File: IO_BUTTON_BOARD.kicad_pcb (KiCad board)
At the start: 2 copper layers, 80 x 40 mm, 113 parts, among them P1 I2C, P10 IO_7, P2 I2C, P3 IO_0, P4 IO_1, P5 IO_2, P6 IO_3, P7 IO_4, P8 IO_5, P9 IO_6, Q1 NPN, Q10 PNP, Q11 PNP, Q12 PNP, Q13 PNP, Q2 PNP, Q3 NPN, Q4 PNP, Q5 NPN, Q6 PNP, Q7 PNP, Q8 PNP, Q9 PNP, SW1 I2C_ADDR, SW2 SW_0, SW3 SW_1, SW4 SW_2, SW5 SW_3, SW6 SW_4, SW7 SW_5, SW8 SW_6, SW9 SW_7, U1 PCF8574A, U2 74HC86, U3 74HC86

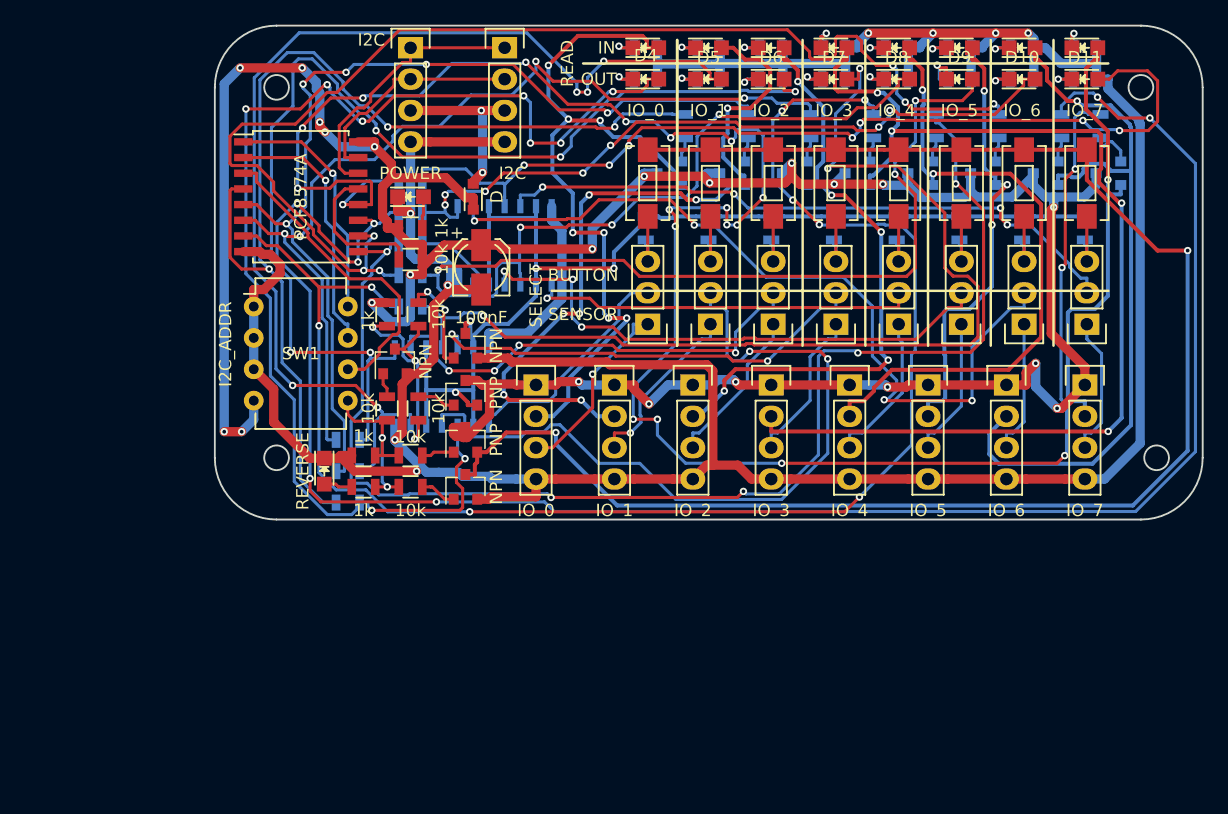
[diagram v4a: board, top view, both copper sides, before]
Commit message: Change positions of components Add mounting holes footprints Rerouted PCB
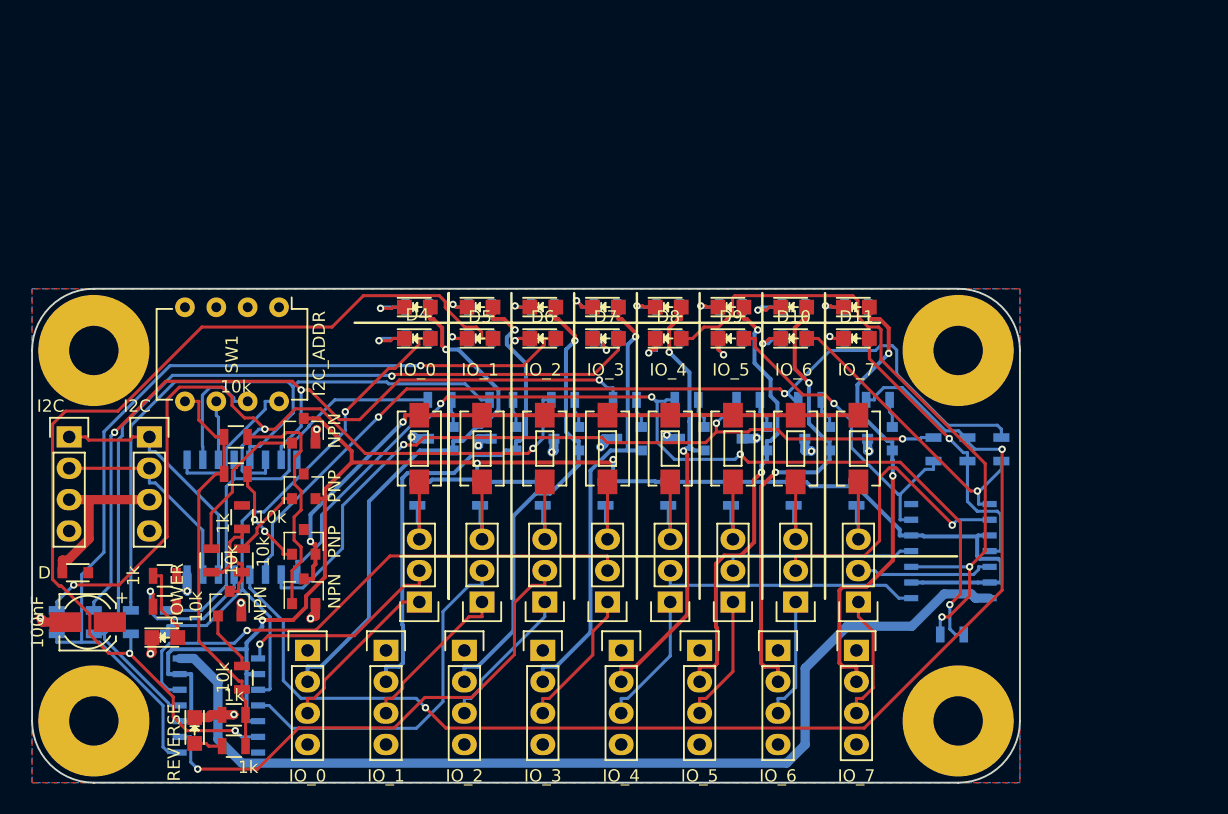
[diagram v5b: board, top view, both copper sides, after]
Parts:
- added REF01: MountingHole_4.3mm_M4, Mounting_Holes:MountingHole_4.3mm_M4, F.Cu at (105.0, 105.0)
- added REF02: MountingHole_4.3mm_M4, Mounting_Holes:MountingHole_4.3mm_M4, F.Cu at (105.0, 135.0)
- added REF03: MountingHole_4.3mm_M4, Mounting_Holes:MountingHole_4.3mm_M4, F.Cu at (175.0, 135.0)
- added REF04: MountingHole_4.3mm_M4, Mounting_Holes:MountingHole_4.3mm_M4, F.Cu at (175.0, 105.0)
- U1: moved to B.Cu
- moved R30 54.1 mm to (174.5, 128.0), turned to 180 degrees
- moved R28 51.6 mm to (178.5, 113.0), turned to 270 degrees
- moved R27 50.1 mm to (175.8, 113.0), turned to 270 degrees
- moved R29 44.6 mm to (173.0, 113.0), turned to 270 degrees
- moved D2 44.3 mm to (103.5, 123.0), turned to 180 degrees
- moved U3 44.0 mm to (174.5, 121.2), turned to 90 degrees
- moved C1 42.9 mm to (104.5, 127.0), turned to 180 degrees
- moved P1 42.7 mm to (109.5, 112.0)
- moved P2 41.9 mm to (103.0, 112.0)
- moved D3 40.9 mm to (110.8, 128.2)
- moved R31 36.2 mm to (105.0, 127.0), turned to 270 degrees
- moved R7 34.5 mm to (110.8, 123.2), turned to 180 degrees
- moved R10 34.4 mm to (110.8, 125.8)
- moved U2 31.7 mm to (115.0, 133.8), turned to 270 degrees
- moved R41 30.1 mm to (163.0, 109.0), turned to 180 degrees
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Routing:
- net GND: track 269.8 -> 10.7 mm, vias 8 -> 6
- net +5V: track 237.6 -> 12.5 mm, vias 22 -> 9
- net Net-(R28-Pad1): track 151.8 -> 75.4 mm, vias 7 -> 2
- net /CONTACT_LANE: track 130.4 -> 54.3 mm
- net Net-(R27-Pad1): track 165.7 -> 99.5 mm, vias 20 -> 2
- net VCC: track 16.0 -> 81.2 mm
- net Net-(R31-Pad1): track 126.4 -> 67.4 mm, vias 8 -> 3
- net Net-(D11-Pad2): track 75.7 -> 23.7 mm, vias 7 -> 1
- net Net-(D4-Pad2): track 97.8 -> 46.0 mm, vias 9 -> 1
- net /OUT_3: track 88.0 -> 36.7 mm, vias 4 -> 1
- net Net-(R34-Pad1): track 86.5 -> 35.5 mm, vias 3 -> 0
- net Net-(S8-Pad2): track 51.9 -> 11.1 mm, vias 4 -> 0
- net Net-(D9-Pad2): track 67.1 -> 26.8 mm, vias 3 -> 1
- net Net-(S7-Pad2): track 65.0 -> 25.0 mm, vias 4 -> 1
- net /PULL_LANE: track 94.2 -> 130.9 mm, vias 4 -> 3
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- added copper zone on F.Cu, net +5V
- added copper zone on B.Cu, net GND
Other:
- outline, holes or cut-outs redrawn
- board text removed: "BUTTON"
- board text removed: "IN"
- board text removed: "OUT"
- board text removed: "READ"
- board text removed: "SELECT"
- board text removed: "SENSOR"

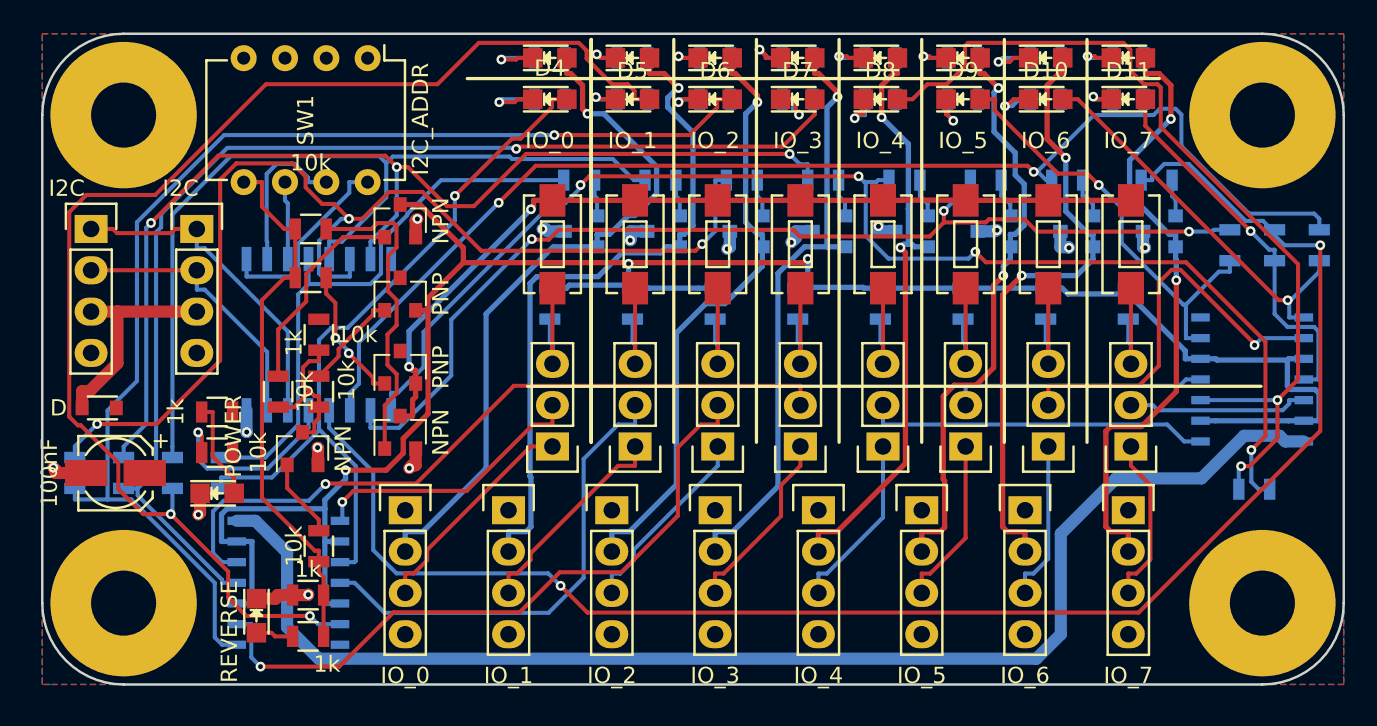
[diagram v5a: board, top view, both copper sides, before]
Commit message: Fix VCC disconnected issue Rerouted with larger width
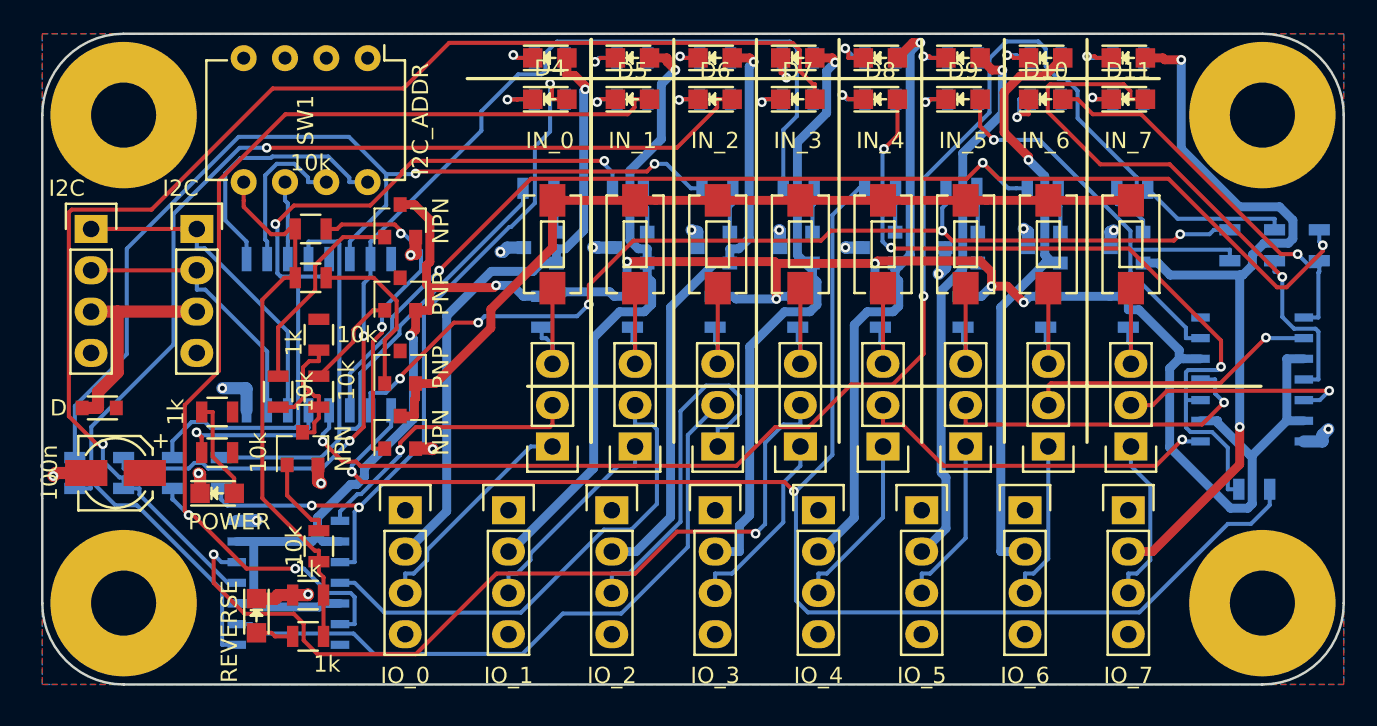
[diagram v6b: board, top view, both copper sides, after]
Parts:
- C1: value 100nF -> 100n
- D10: value IO_6 -> IN_6
- D11: value IO_7 -> IN_7
- D4: value IO_0 -> IN_0
- D5: value IO_1 -> IN_1
- D6: value IO_2 -> IN_2
- D7: value IO_3 -> IN_3
- D8: value IO_4 -> IN_4
- D9: value IO_5 -> IN_5
- moved Q6 2.69 mm to (130.6, 113.1)
- moved R35 2.55 mm to (130.5, 109.5)
- moved Q10 2.24 mm to (151.4, 113.1)
- moved Q11 2.24 mm to (156.5, 113.1)
- moved Q12 2.24 mm to (161.6, 113.1)
- moved Q13 2.24 mm to (166.7, 113.1)
- moved Q7 2.24 mm to (136.2, 113.1)
- moved Q8 2.24 mm to (141.3, 113.1)
- moved Q9 2.24 mm to (146.3, 113.1)
- moved R36 2.06 mm to (136.0, 109.5)
- moved R37 1.58 mm to (141.5, 109.5)
- moved R38 1.58 mm to (146.5, 109.5)
- moved R39 1.58 mm to (151.5, 109.5)
- moved R40 1.58 mm to (156.5, 109.5)
- moved R41 1.58 mm to (161.5, 109.5)
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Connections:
- U2 pad 14: VCC -> +5V
- U3 pad 14: VCC -> +5V
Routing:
- net VCC: track 81.2 -> 0.00 mm
- net Net-(D11-Pad2): track 23.7 -> 37.1 mm
- net Net-(R30-Pad1): track 80.0 -> 93.0 mm, vias 4 -> 2
- net Net-(D5-Pad2): track 80.0 -> 67.3 mm
- net Net-(R27-Pad1): track 99.5 -> 87.5 mm
- net /OUT_7: track 38.1 -> 49.1 mm
- net Net-(D7-Pad2): track 70.9 -> 81.2 mm
- net /IN_2: track 12.0 -> 22.0 mm
- net Net-(R32-Pad1): track 69.5 -> 60.3 mm, vias 3 -> 2
- net Net-(D8-Pad2): track 55.0 -> 47.0 mm, vias 2 -> 3
- net Net-(R34-Pad1): track 35.5 -> 42.9 mm
- net Net-(S4-Pad2): track 44.7 -> 51.9 mm, vias 1 -> 2
- net Net-(S7-Pad2): track 25.0 -> 18.1 mm
- net /PULL_LANE: track 130.9 -> 137.3 mm, vias 3 -> 7
- net /OUT_0: track 42.6 -> 38.1 mm
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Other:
- net class Alim added: clearance 0.2, trace_width 1, via_dia 0.6, via_drill 0.4

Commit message: Reroute PCB with 'fake' +5V and GND netlist in order to get different width for PCB tracks
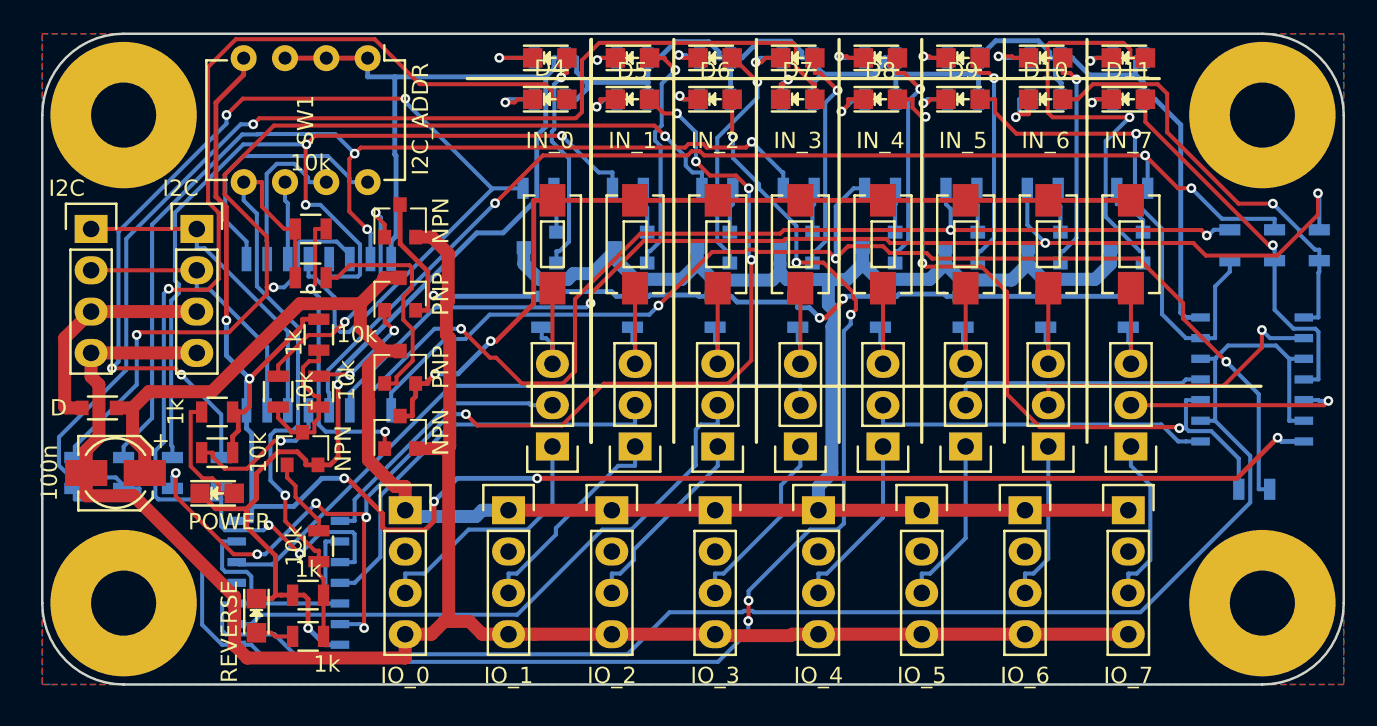
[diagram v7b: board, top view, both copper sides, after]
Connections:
- C1 pad 1: +5V -> /5V_PWR
- C1 pad 2: GND -> /GND_PWR
- D12 pad 2: /OUT_0 -> /D_OUT_0
- D13 pad 2: /OUT_1 -> /D_OUT_1
- D14 pad 2: /OUT_2 -> /D_OUT_2
- D15 pad 2: /OUT_3 -> /D_OUT_3
- D16 pad 2: /OUT_4 -> /D_OUT_4
- D17 pad 2: /OUT_5 -> /D_OUT_5
- D18 pad 2: /OUT_6 -> /D_OUT_6
- D19 pad 2: /OUT_7 -> /D_OUT_7
- D2 pad 1: +5V -> /5V_PWR
- P1 pad 4: GND -> /GND_PWR
- P10 pad 1: +5V -> /5V_PWR
- P10 pad 4: GND -> /GND_PWR
- P2 pad 4: GND -> /GND_PWR
- P3 pad 1: +5V -> /5V_PWR
- P3 pad 4: GND -> /GND_PWR
- P4 pad 1: +5V -> /5V_PWR
- P4 pad 4: GND -> /GND_PWR
- P5 pad 1: +5V -> /5V_PWR
- P5 pad 4: GND -> /GND_PWR
- P6 pad 1: +5V -> /5V_PWR
- P6 pad 4: GND -> /GND_PWR
- P7 pad 1: +5V -> /5V_PWR
- P7 pad 4: GND -> /GND_PWR
- P8 pad 1: +5V -> /5V_PWR
- P8 pad 4: GND -> /GND_PWR
- P9 pad 1: +5V -> /5V_PWR
- P9 pad 4: GND -> /GND_PWR
- Q10 pad 2: /OUT_4 -> /D_OUT_4
- Q10 pad 3: +5V -> /5V_PWR
- Q11 pad 2: /OUT_5 -> /D_OUT_5
- Q11 pad 3: +5V -> /5V_PWR
- Q12 pad 2: /OUT_6 -> /D_OUT_6
- Q12 pad 3: +5V -> /5V_PWR
- Q13 pad 2: /OUT_7 -> /D_OUT_7
- Q13 pad 3: +5V -> /5V_PWR
- Q2 pad 3: +5V -> /5V_PWR
- Q3 pad 2: GND -> /GND_PWR
- Q4 pad 3: +5V -> /5V_PWR
- Q5 pad 2: GND -> /GND_PWR
- Q6 pad 2: /OUT_0 -> /D_OUT_0
- Q6 pad 3: +5V -> /5V_PWR
- Q7 pad 2: /OUT_1 -> /D_OUT_1
- Q7 pad 3: +5V -> /5V_PWR
- Q8 pad 2: /OUT_2 -> /D_OUT_2
- Q8 pad 3: +5V -> /5V_PWR
- Q9 pad 2: /OUT_3 -> /D_OUT_3
- Q9 pad 3: +5V -> /5V_PWR
- R10 pad 2: +5V -> VCC
- R4 pad 1: +5V -> VCC
- R7 pad 1: +5V -> VCC
- SW1 pad 4: +5V -> VCC
- U1 pad 16: +5V -> VCC
- U2 pad 10: /PULL_LANE -> /PULL_LANE_D
- U2 pad 13: /PULL_LANE -> /PULL_LANE_D
- U2 pad 14: +5V -> VCC
- U2 pad 2: /PULL_LANE -> /PULL_LANE_D
- U2 pad 5: /PULL_LANE -> /PULL_LANE_D
- U3 pad 10: /PULL_LANE -> /PULL_LANE_D
- U3 pad 13: /PULL_LANE -> /PULL_LANE_D
- U3 pad 14: +5V -> VCC
- U3 pad 2: /PULL_LANE -> /PULL_LANE_D
- U3 pad 5: /PULL_LANE -> /PULL_LANE_D
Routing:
- net GND: track 10.4 -> 162.7 mm, vias 6 -> 2
- net /5V_PWR: track 0.00 -> 150.5 mm
- net /GND_PWR: track 0.00 -> 115.2 mm
- net VCC: track 0.00 -> 113.0 mm, vias 0 -> 6
- net /PULL_LANE_D: track 0.00 -> 109.9 mm
- net /PULL_LANE: track 137.3 -> 53.3 mm, vias 7 -> 3
- net /OUT_7: track 49.1 -> 0.00 mm, vias 2 -> 0
- net /OUT_1: track 38.3 -> 0.00 mm, vias 1 -> 0
- net /OUT_0: track 38.1 -> 0.00 mm, vias 1 -> 0
- net /OUT_3: track 37.8 -> 0.00 mm, vias 1 -> 0
- net /OUT_6: track 37.5 -> 0.00 mm, vias 1 -> 0
- net /OUT_4: track 37.3 -> 0.00 mm, vias 1 -> 0
- net /OUT_2: track 36.9 -> 0.00 mm, vias 1 -> 0
- net /OUT_5: track 34.5 -> 0.00 mm, vias 1 -> 0
- net /D_OUT_7: track 0.00 -> 26.7 mm, vias 0 -> 1
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- added copper zone on B.Cu, net /GND_PWR
- added copper zone on F.Cu, net /GND_PWR
- removed copper zone on F.Cu, net +5V
- removed copper zone on B.Cu, net GND
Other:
- net class Alim removed
- net class digital_signal added: clearance 0.2, trace_width 0.25, via_dia 0.6, via_drill 0.4
- net class high_current added: clearance 0.2, trace_width 0.5, via_dia 0.6, via_drill 0.4
- net class low_current added: clearance 0.2, trace_width 0.3, via_dia 0.6, via_drill 0.4
- net class power_track added: clearance 0.2, trace_width 0.8, via_dia 0.6, via_drill 0.4

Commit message: Change silkscreen layout and 3D models
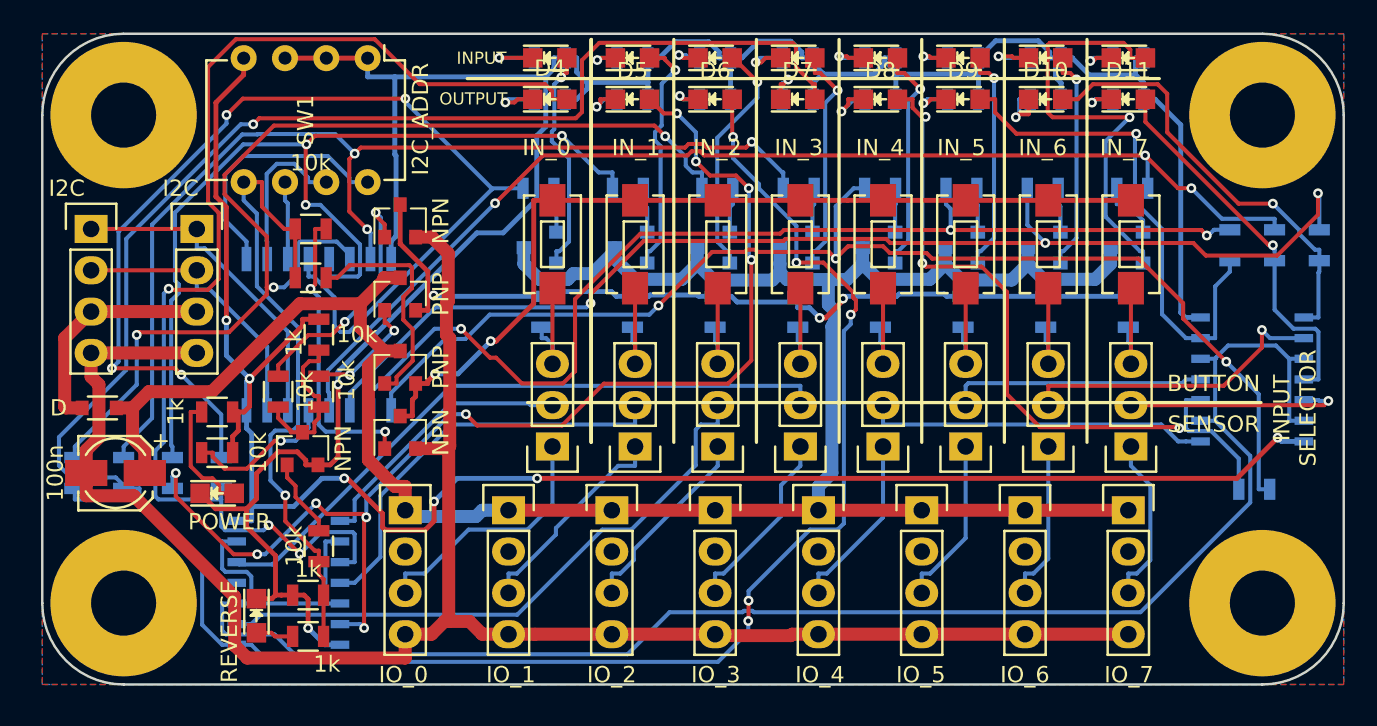
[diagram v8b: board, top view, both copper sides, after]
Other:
- board text added: "BUTTON"
- board text added: "INPUT"
- board text added: "INPUT SELECTOR"
- board text added: "OUTPUT"
- board text added: "SENSOR"
